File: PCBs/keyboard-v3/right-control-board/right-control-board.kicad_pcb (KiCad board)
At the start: 4 copper layers, 111.9 x 40 mm, 69 parts, among them J201 USB4510-03-1-A, J202 USB4510-03-1-A, J203 USB4510-03-1-A, J204 GSB12J21C1EU, J501 Conn_02x08_Odd_Even, J601 F31Z1A7H111008, J602 F31Z1A7H111008, J701 Conn_01x02, U201 USBLC6-4SC6, U202 USBLC6-4SC6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

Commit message: Moved charging LED
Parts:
- moved D701 1.13 mm to (130.7, 79.2)
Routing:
- net /Power/STAT1: track 44.7 -> 45.3 mm
- net GND: vias 93 -> 98
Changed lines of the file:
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@@
 	(footprint "project_footprints:LED_0402"
 		(layer "F.Cu")
-		(at 131.5 80 90)
+		(at 130.7 79.2 90)
 		(descr "LED SMD 0402 (1005 Metric), square (rectangular) end terminal, IPC-7351 nominal, (Body size source: http://www.tortai-tech.com/upload/download/2011102023233369053.pdf), generated with kicad-footprint-generator")
 		(tags "LED")
@@
 	)
 	(via
+		(at 174 85)
+		(size 0.45)
+		(drill 0.3)
+		(layers "F.Cu" "B.Cu")
+		(free yes)
+		(net 39)
+	)
+	(via
 		(at 122.35 102.85)
 		(size 0.45)
@@
 	)
 	(via
+		(at 156 85)
+		(size 0.45)
+		(drill 0.3)
+		(layers "F.Cu" "B.Cu")
+		(free yes)
+		(net 39)
+	)
+	(via
 		(at 103.5 116.4)
 		(size 0.45)
@@
 	)
 	(via
+		(at 192 85)
+		(size 0.45)
+		(drill 0.3)
+		(layers "F.Cu" "B.Cu")
+		(free yes)
+		(net 39)
+	)
+	(via
 		(at 117.8 105)
 		(size 0.45)
@@
 	)
 	(via
+		(at 164 85)
+		(size 0.45)
+		(drill 0.3)
+		(layers "F.Cu" "B.Cu")
+		(free yes)
+		(net 39)
+	)
+	(via
 		(at 168.5 91.5)
 		(size 0.45)
@@
 	)
 	(via
+		(at 182 85)
+		(size 0.45)
+		(drill 0.3)
+		(layers "F.Cu" "B.Cu")
+		(free yes)
+		(net 39)
+	)
+	(via
 		(at 125.625 106.925)
 		(size 0.45)
@@
 	)
 	(segment
-		(start 130.5 81.485)
-		(end 131.5 80.485)
+		(start 130.5 79.885)
+		(end 130.7 79.685)
 		(width 0.15)
 		(layer "F.Cu")
@@
 	)
 	(segment
+		(start 130.5 93.8)
+		(end 130.5 79.885)
+		(width 0.15)
+		(layer "F.Cu")
+		(net 85)
+	)
+	(segment
 		(start 133 111.4)
 		(end 133 115.3)
@@
 	)
 	(segment
-		(start 130.5 93.8)
-		(end 130.5 81.485)
+		(start 131.1 94.4)
+		(end 130.5 93.8)
 		(width 0.15)
 		(layer "F.Cu")
@@
 		(net 85)
 	)
-	(segment
-		(start 131.1 94.4)
-		(end 130.5 93.8)
-		(width 0.15)
-		(layer "F.Cu")
-		(net 85)
-	)
 	(via
 		(at 130.5 104.4)
@@
 	)
 	(segment
-		(start 130.715 79.515)
-		(end 131.5 79.515)
+		(start 131.385 78.715)
+		(end 130.7 78.715)
 		(width 0.15)
 		(layer "F.Cu")
@@
 	)
 	(via
-		(at 130.715 79.515)
+		(at 131.385 78.715)
 		(size 0.45)
 		(drill 0.3)
@@
 	)
 	(segment
-		(start 131.1 104)
-		(end 131.1 98.3)
+		(start 132 93.4)
+		(end 132 97.4)
 		(width 0.15)
 		(layer "B.Cu")
@@
 	)
 	(segment
-		(start 132 93.4)
-		(end 131.1 92.5)
+		(start 131.1 92.5)
+		(end 132 93.4)
 		(width 0.15)
 		(layer "B.Cu")
@@
 	(segment
 		(start 131.1 98.3)
-		(end 132 97.4)
+		(end 131.1 104)
 		(width 0.15)
 		(layer "B.Cu")
@@
 	)
 	(segment
-		(start 131.1 92.5)
-		(end 131.1 79.9)
+		(start 131.385 78.715)
+		(end 131.1 79)
 		(width 0.15)
 		(layer "B.Cu")
@@
 	)
 	(segment
-		(start 132 97.4)
-		(end 132 93.4)
+		(start 131.1 79)
+		(end 131.1 92.5)
 		(width 0.15)
 		(layer "B.Cu")
@@
 	)
 	(segment
-		(start 131.1 79.9)
-		(end 130.715 79.515)
+		(start 132 97.4)
+		(end 131.1 98.3)
 		(width 0.15)
 		(layer "B.Cu")

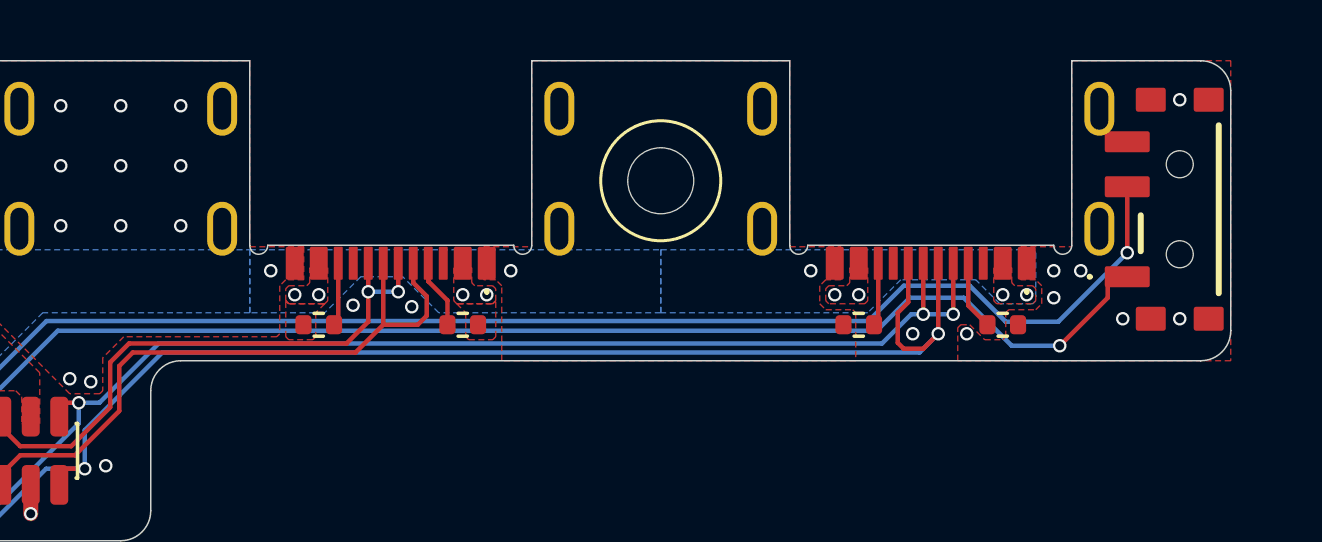
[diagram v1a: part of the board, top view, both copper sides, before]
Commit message: Left key board done
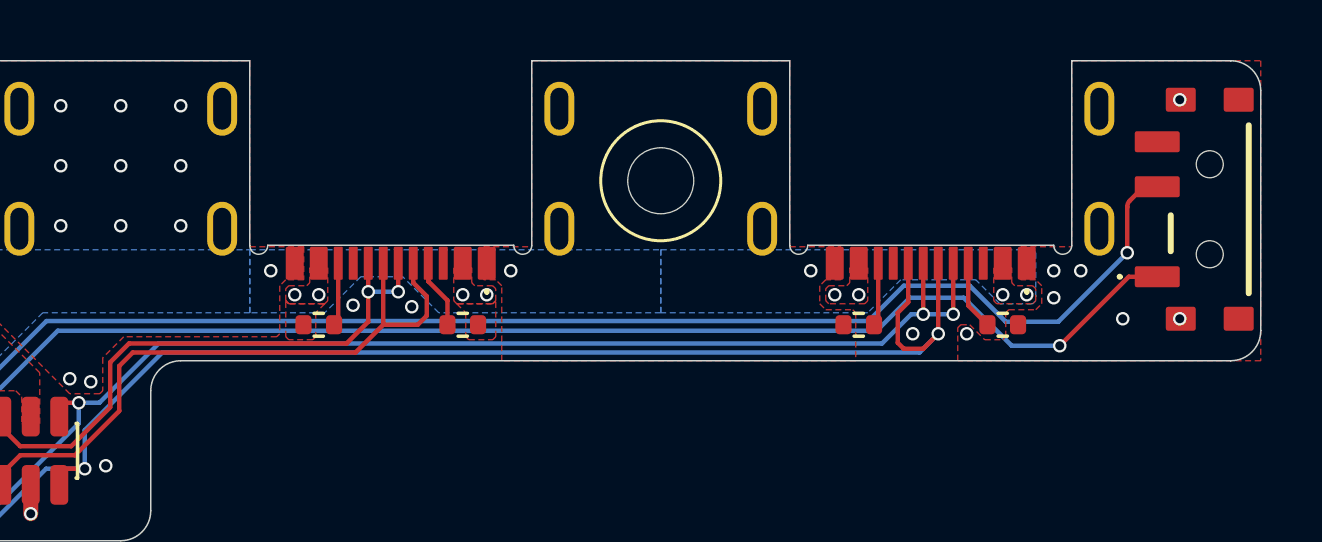
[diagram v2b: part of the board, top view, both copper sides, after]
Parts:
- moved S701 1.00 mm to (205.3, 83.0)
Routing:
- net +VSYS: track 97.2 -> 98.4 mm
- net /Power/EN: track 122.7 -> 123.3 mm
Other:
- board size 111.9 x 40 mm -> 112.9 x 40 mm

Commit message: Left control board done
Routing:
- net GND: vias 98 -> 99
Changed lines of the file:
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@@
 	)
 	(via
-		(at 120.05 102.85)
+		(at 206.2 83)
 		(size 0.45)
 		(drill 0.3)
 		(layers "F.Cu" "B.Cu")
+		(free yes)
 		(net 39)
 	)
 	(via
-		(at 121.2 102.85)
+		(at 120.05 102.85)
 		(size 0.45)
 		(drill 0.3)
@@
 	)
 	(via
-		(at 142 93.9)
+		(at 121.2 102.85)
 		(size 0.45)
 		(drill 0.3)
@@
 	)
 	(via
-		(at 204.3 86.6)
+		(at 142 93.9)
 		(size 0.45)
 		(drill 0.3)
 		(layers "F.Cu" "B.Cu")
-		(free yes)
 		(net 39)
 	)
@@
 	)
 	(via
+		(at 201.7 87.3)
+		(size 0.45)
+		(drill 0.3)
+		(layers "F.Cu" "B.Cu")
+		(free yes)
+		(net 39)
+	)
+	(via
 		(at 139.6 101.5)
 		(size 0.45)
@@
 	)
 	(via
+		(at 203.3 86.6)
+		(size 0.45)
+		(drill 0.3)
+		(layers "F.Cu" "B.Cu")
+		(free yes)
+		(net 39)
+	)
+	(via
 		(at 168 88.7)
 		(size 0.45)
@@
 	)
 	(via
-		(at 202.4 86.6)
-		(size 0.45)
-		(drill 0.3)
-		(layers "F.Cu" "B.Cu")
-		(free yes)
-		(net 39)
-	)
-	(via
 		(at 141.1 100)
 		(size 0.45)
@@
 	)
 	(via
+		(at 203.3 79.3)
+		(size 0.45)
+		(drill 0.3)
+		(layers "F.Cu" "B.Cu")
+		(free yes)
+		(net 39)
+	)
+	(via
 		(at 125.9 101.2)
 		(size 0.45)
@@
 	)
 	(via
-		(at 204.3 79.3)
-		(size 0.45)
-		(drill 0.3)
-		(layers "F.Cu" "B.Cu")
-		(free yes)
-		(net 39)
-	)
-	(via
 		(at 111.5 113.6)
 		(size 0.45)
@@
 		(polygon
 			(pts
-				(xy 206 78) (xy 206 118) (xy 94 118) (xy 94 78)
+				(xy 207 78) (xy 207 118) (xy 94 118) (xy 94 78)
 			)
 		)

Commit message: Keyboard v3 hardware done
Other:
- board text added: "+"
- board text added: "-"
- board text added: "Keyboard v3 Right Control Board Ben Smith 2026"
- board text added: "Off"
- board text added: "On"
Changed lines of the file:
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@@
 			(sketchdnponfab yes)
 			(crossoutdnponfab yes)
-			(subtractmaskfromsilk no)
+			(subtractmaskfromsilk yes)
 			(outputformat 1)
 			(mirror no)
-			(drillshape 1)
+			(drillshape 0)
 			(scaleselection 1)
-			(outputdirectory "")
+			(outputdirectory "gerbers/")
 		)
 	)
@@
 		(layer "Edge.Cuts")
 	)
+	(gr_text "-"
+		(at 146.3 107.4 0)
+		(layer "F.SilkS")
+		(effects
+			(font
+				(size 1 1)
+				(thickness 0.1)
+			)
+		)
+	)
+	(gr_text "+"
+		(at 146.3 109.5 0)
+		(layer "F.SilkS")
+		(effects
+			(font
+				(size 1 1)
+				(thickness 0.1)
+			)
+		)
+	)
+	(gr_text "Off"
+		(at 206 80 90)
+		(layer "B.SilkS")
+		(effects
+			(font
+				(size 1 1)
+				(thickness 0.1)
+			)
+			(justify mirror)
+		)
+	)
+	(gr_text "Keyboard v3\nRight Control Board\nBen Smith 2026"
+		(at 119.9 109.3 0)
+		(layer "B.SilkS")
+		(effects
+			(font
+				(size 1 1)
+				(thickness 0.1)
+			)
+			(justify mirror)
+		)
+	)
+	(gr_text "On"
+		(at 206 86 90)
+		(layer "B.SilkS")
+		(effects
+			(font
+				(size 1 1)
+				(thickness 0.1)
+			)
+			(justify mirror)
+		)
+	)
 	(dimension

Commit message: Added v3 left BOMs and updated buck inductor
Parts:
- L701: value 78438313015 -> 74438313015; footprint project_footprints:L_Wurth_WE-MAIA-1610 -> project_footprints:L_Wurth_WE-MAPI-1610
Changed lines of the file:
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@@
 		)
 	)
-	(footprint "project_footprints:L_Wurth_WE-MAIA-1610"
+	(footprint "project_footprints:L_Wurth_WE-MAPI-1610"
 		(layer "F.Cu")
 		(at 104.5 105 180)
-		(descr "Single Coil Power Inductor, body 1.6x1.6x1mm, https://www.we-online.com/en/components/products/WE-MAIA#/articles/WE_MAIA_SIZE_1610")
+		(descr "Shielded Power Inductor, body 1.6x1.6mm, https://www.we-online.com/catalog/en/WE-MAPI#/articles/WE-MAPI-1610")
 		(tags "SMT")
 		(property "Reference" "L701"
-			(at 0 -2.15 180)
+			(at 0 -1.8 180)
 			(unlocked yes)
 			(layer "F.SilkS")
@@
 			)
 		)
-		(property "Value" "78438313015"
-			(at 0 2.15 180)
-			(unlocked yes)
-			(layer "F.Fab")
-			(hide yes)
-			(effects
-				(font
-					(size 1 1)
-					(thickness 0.15)
-				)
-			)
-		)
-		(property "Datasheet" "https://www.we-online.com/catalog/datasheet/78438313015.pdf?ki"
-			(at 0 0 0)
+		(property "Value" "74438313015"
+			(at 0 1.9 180)
+			(unlocked yes)
+			(layer "F.Fab")
+			(effects
+				(font
+					(size 1 1)
+					(thickness 0.15)
+				)
+			)
+		)
+		(property "Datasheet" "https://www.we-online.com/catalog/datasheet/74438313015.pdf?ki"
+			(at 0 0 180)
 			(layer "F.Fab")
 			(hide yes)
@@
 			)
 		)
-		(property "Description" "Single Coil Power Inductor"
-			(at 0 0 0)
+		(property "Description" "Shielded Power Inductor"
+			(at 0 0 180)
 			(layer "F.Fab")
 			(hide yes)
@@
 			)
 		)
-		(property "Published Date" "20250429"
-			(at 0 0 180)
-			(unlocked yes)
-			(layer "F.Fab")
-			(hide yes)
-			(effects
-				(font
-					(size 1 1)
-					(thickness 0.15)
-				)
-			)
-		)
-		(property "Match Code" "WE-MAIA"
-			(at 0 0 180)
-			(unlocked yes)
-			(layer "F.Fab")
-			(hide yes)
-			(effects
-				(font
-					(size 1 1)
-					(thickness 0.15)
-				)
-			)
-		)
-		(property "Part Number" "78438313015"
+		(property "Published Date" "20250320"
+			(at 0 0 180)
+			(unlocked yes)
+			(layer "F.Fab")
+			(hide yes)
+			(effects
+				(font
+					(size 1 1)
+					(thickness 0.15)
+				)
+			)
+		)
+		(property "Match Code" "WE-MAPI"
+			(at 0 0 180)
+			(unlocked yes)
+			(layer "F.Fab")
+			(hide yes)
+			(effects
+				(font
+					(size 1 1)
+					(thickness 0.15)
+				)
+			)
+		)
+		(property "Part Number" "74438313015"
 			(at 0 0 180)
 			(unlocked yes)
@@
 			)
 		)
-		(property ki_fp_filters "*WE-MAIA*1610*")
+		(property "RDC typ. (mΩ)" "189.0"
+			(at 0 0 180)
+			(unlocked yes)
+			(layer "F.Fab")
+			(hide yes)
+			(effects
+				(font
+					(size 1 1)
+					(thickness 0.15)
+				)
+			)
+		)
+		(property "VOP (V)" "80"
+			(at 0 0 180)
+			(unlocked yes)
+			(layer "F.Fab")
+			(hide yes)
+			(effects
+				(font
+					(size 1 1)
+					(thickness 0.15)
+				)
+			)
+		)
+		(property ki_fp_filters "*WE-MAPI*1610*")
 		(sheetname "/Power/")
 		(sheetfile "power.kicad_sch")
@@
 			(layer "F.CrtYd")
 		)
-		(fp_rect
+		(fp_line
+			(start 0.8 -0.8)
+			(end 0.8 0.8)
+			(stroke
+				(width 0.1)
+				(type solid)
+			)
+			(layer "F.Fab")
+		)
+		(fp_line
+			(start -0.8 0.8)
+			(end 0.8 0.8)
+			(stroke
+				(width 0.1)
+				(type solid)
+			)
+			(layer "F.Fab")
+		)
+		(fp_line
+			(start -0.8 0.8)
+			(end -0.8 -0.8)
+			(stroke
+				(width 0.1)
+				(type solid)
+			)
+			(layer "F.Fab")
+		)
+		(fp_line
 			(start -0.8 -0.8)
-			(end 0.8 0.8)
+			(end 0.8 -0.8)
 			(stroke
 				(width 0.1)
 				(type solid)
 			)
-			(fill no)
-			(layer "F.Fab")
+			(layer "F.Fab")
+		)
+		(fp_text user "Solder Resist"
+			(at 0 -1 180)
+			(unlocked yes)
+			(layer "Cmts.User")
+			(effects
+				(font
+					(size 0.5 0.5)
+					(thickness 0.075)
+				)
+			)
 		)
 		(fp_text user "${REFERENCE}"
@@
 			(net 0)
 			(net_name "")
-			(layer "F.Cu")
+			(layers "F.Cu" "Dwgs.User")
 			(name "Solder Resist")
 			(hatch full 0.1)
@@
 			(polygon
 				(pts
-					(xy 104.7 105.85) (xy 104.7 104.15) (xy 104.65 104.1) (xy 104.35 104.1) (xy 104.3 104.15) (xy 104.3 105.85)
-					(xy 104.35 105.9) (xy 104.65 105.9)
+					(xy 104.7 106.15) (xy 104.7 103.85) (xy 104.3 103.85) (xy 104.3 106.15)
 				)
 			)
 		)
 		(embedded_fonts no)
-		(model "${KIPRJMOD}/../component-library/project_models/L_Wurth_WE-MAIA-1610.step"
+		(model "${KIPRJMOD}/../component-library/project_models/L_Wurth_WE-MAPI-1610.step"
 			(offset
 				(xyz 0 0 0)
